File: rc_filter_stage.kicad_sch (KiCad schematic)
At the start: 2 parts

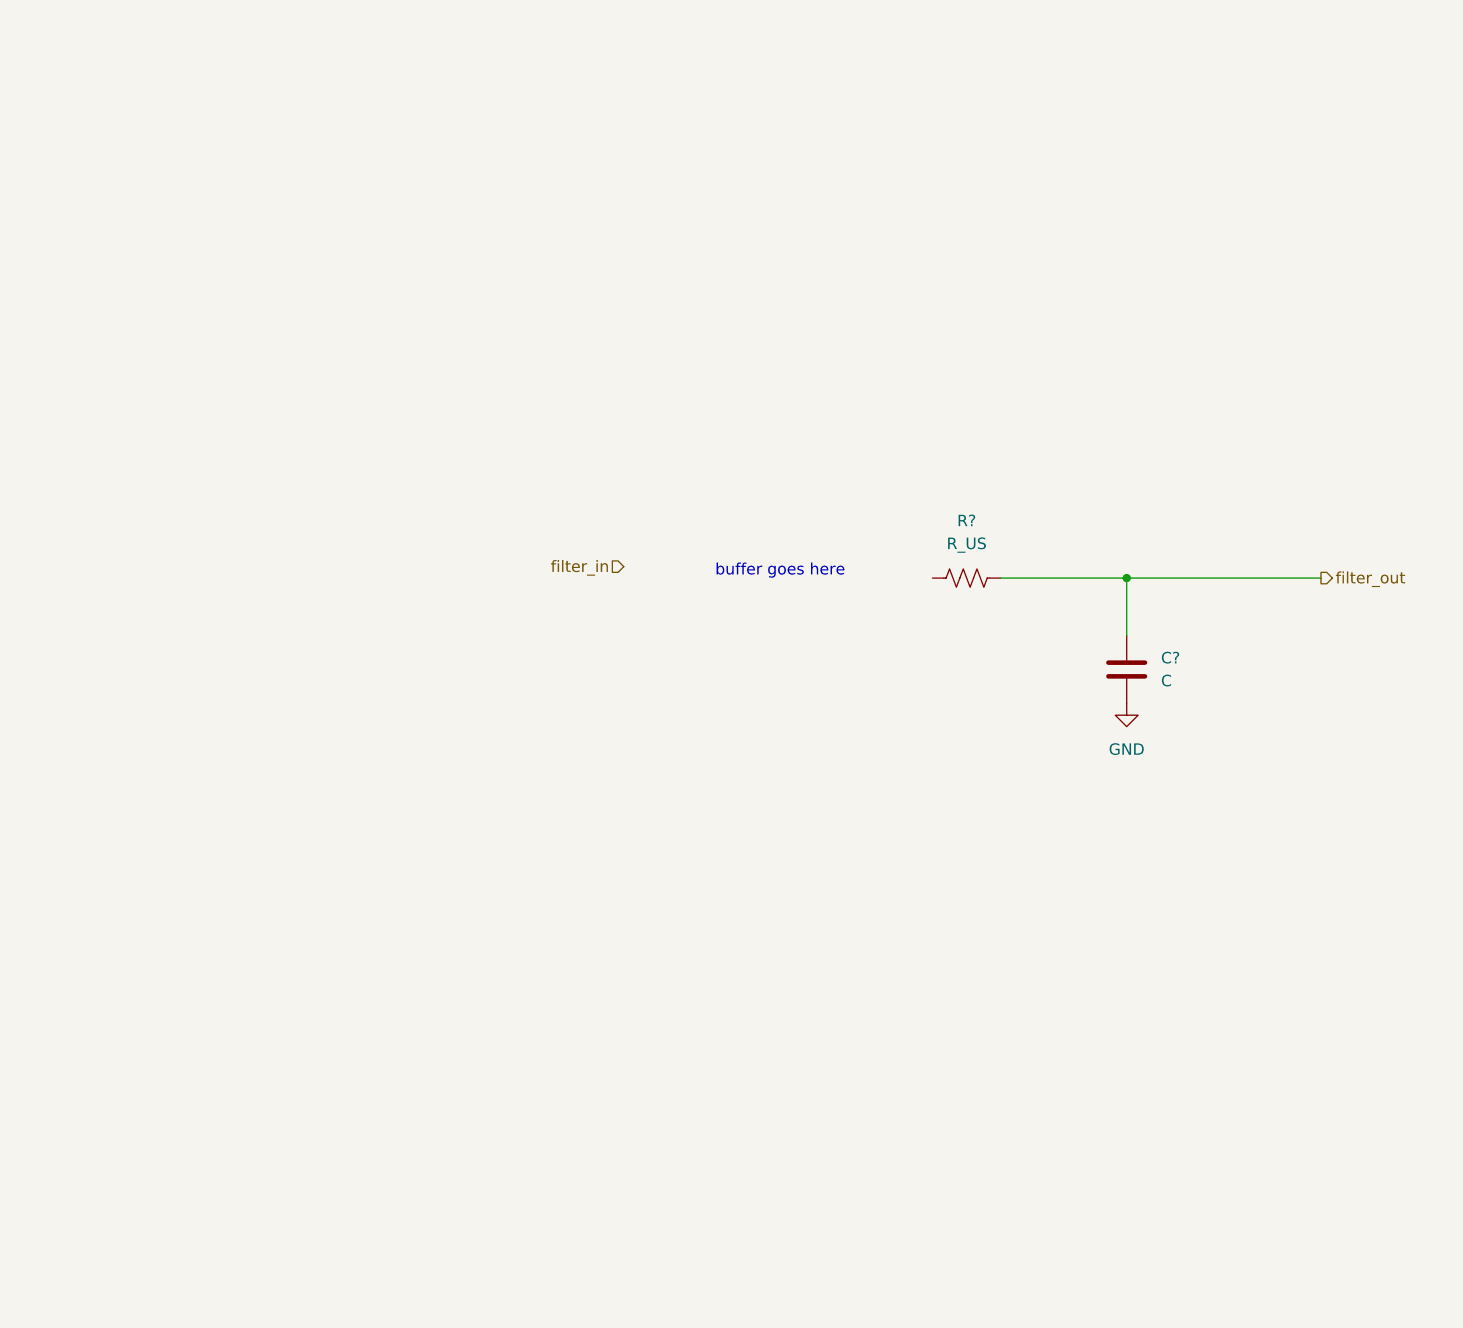
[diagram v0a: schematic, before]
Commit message: Added amplifier to rc filter
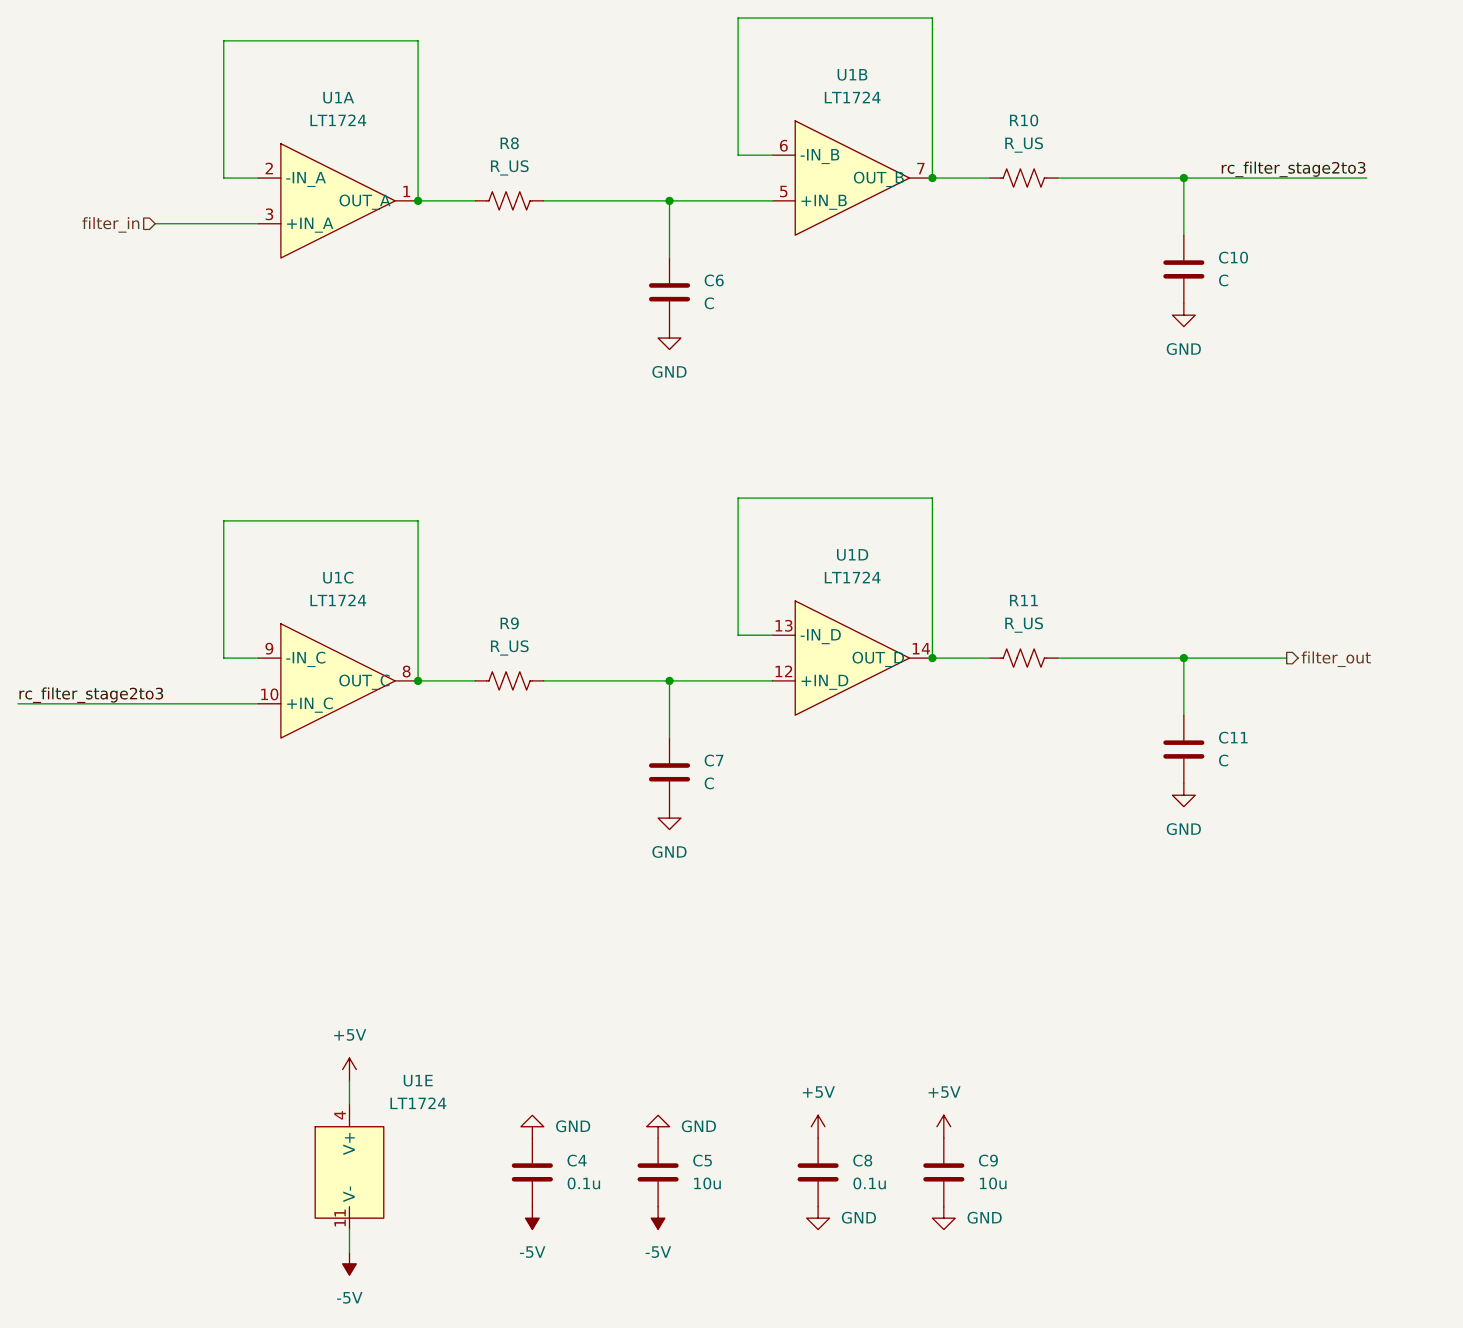
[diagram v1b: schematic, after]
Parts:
- added C10, C11, C7: C, symbol Device:C
- added C4, C8: 0.1u, symbol Device:C
- added C5, C9: 10u, symbol Device:C
- added R10, R11, R9: R_US, symbol Device:R_US
- added U1: LT1724, Package_SO:SOIC-14_3.9x8.7mm_P1.27mm, symbol My_Lib:LT1724
- gave numbers to parts that had none: 2
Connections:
- net GND: now also C10.2, C11.2, C4.1, C5.1, C7.2, C8.2, C9.2
- net filter_in: now also U1.3 (+IN_A)
- net filter_out: now also C11.1, R11.2; no longer C6.1, R8.2
- net at R8.1: now also U1.1 (OUT_A), U1.2 (-IN_A)
- new net: C6.1, R8.2, U1.5 (+IN_B)
- new net: R10.1, U1.6 (-IN_B), U1.7 (OUT_B)
- new net: C7.1, R9.2, U1.12 (+IN_D)
- new net: R11.1, U1.13 (-IN_D), U1.14 (OUT_D)
- new net: R9.1, U1.8 (OUT_C), U1.9 (-IN_C)
- new net +5V: C8.1, C9.1, U1.4 (V+)
- new net -5V: C4.2, C5.2, U1.11 (V-)
- new net rc_filter_stage2to3: C10.1, R10.2, U1.10 (+IN_C)
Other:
- note removed: "buffer goes here"
- moved on the sheet: C6, R8
